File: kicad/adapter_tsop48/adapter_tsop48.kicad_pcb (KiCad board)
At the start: 2 copper layers, 48 x 33 mm, 3 parts, among them J1 Conn_02x12_Odd_Even_1, J2 Conn_02x12_Odd_Even_2, P1 TSOP-48_adapter

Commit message: upgrade project files to kicad version 6.0.11
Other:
- net class Default removed

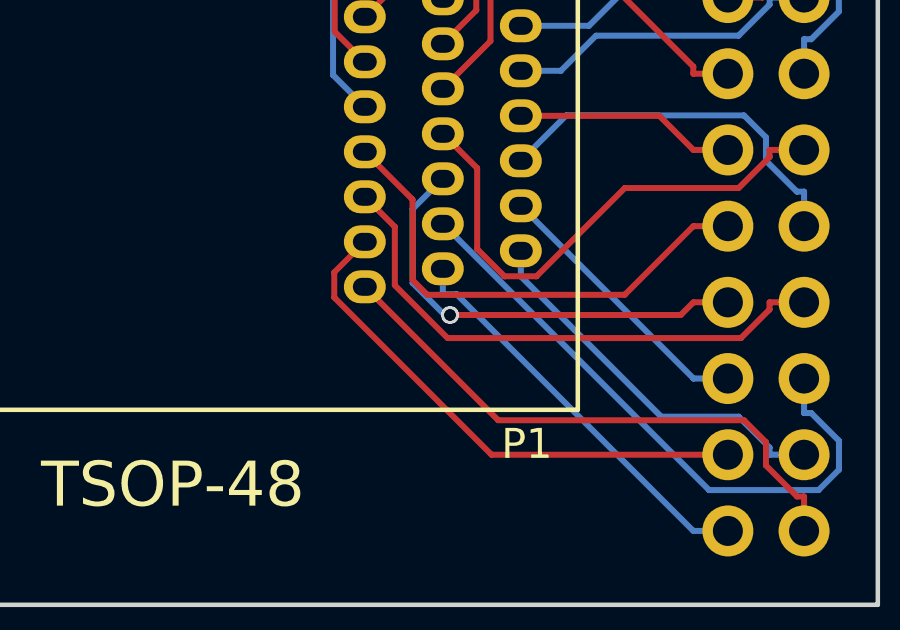
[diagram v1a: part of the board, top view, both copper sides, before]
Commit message: Revert "upgrade project files to kicad version 6.0.11"
This reverts commit 6c6c989fefeeef77173a4749b3826cd3583d0fba.
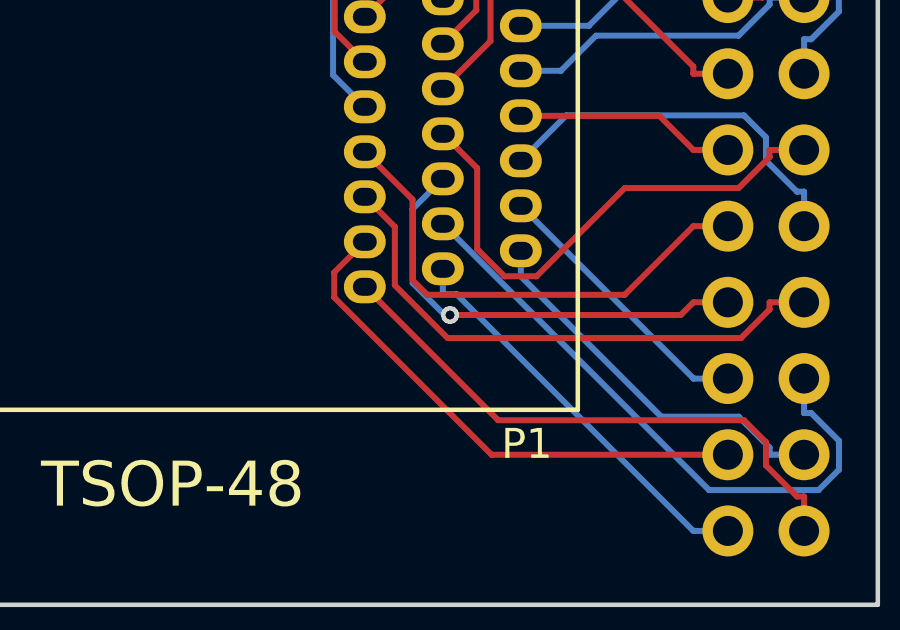
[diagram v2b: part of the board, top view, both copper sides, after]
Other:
- net class Default added: clearance 0.2, trace_width 0.2, via_dia 0.6, via_drill 0.4
